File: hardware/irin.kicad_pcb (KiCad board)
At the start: 2 copper layers, 78.5 x 69 mm, 15 parts, among them J1 12V IN, J2 DHT22, U1 MP1584EN set to 5.0V, U2 01Space ESP32-C3-0.42LCD, U3 ADS1115 (HiLetgo)

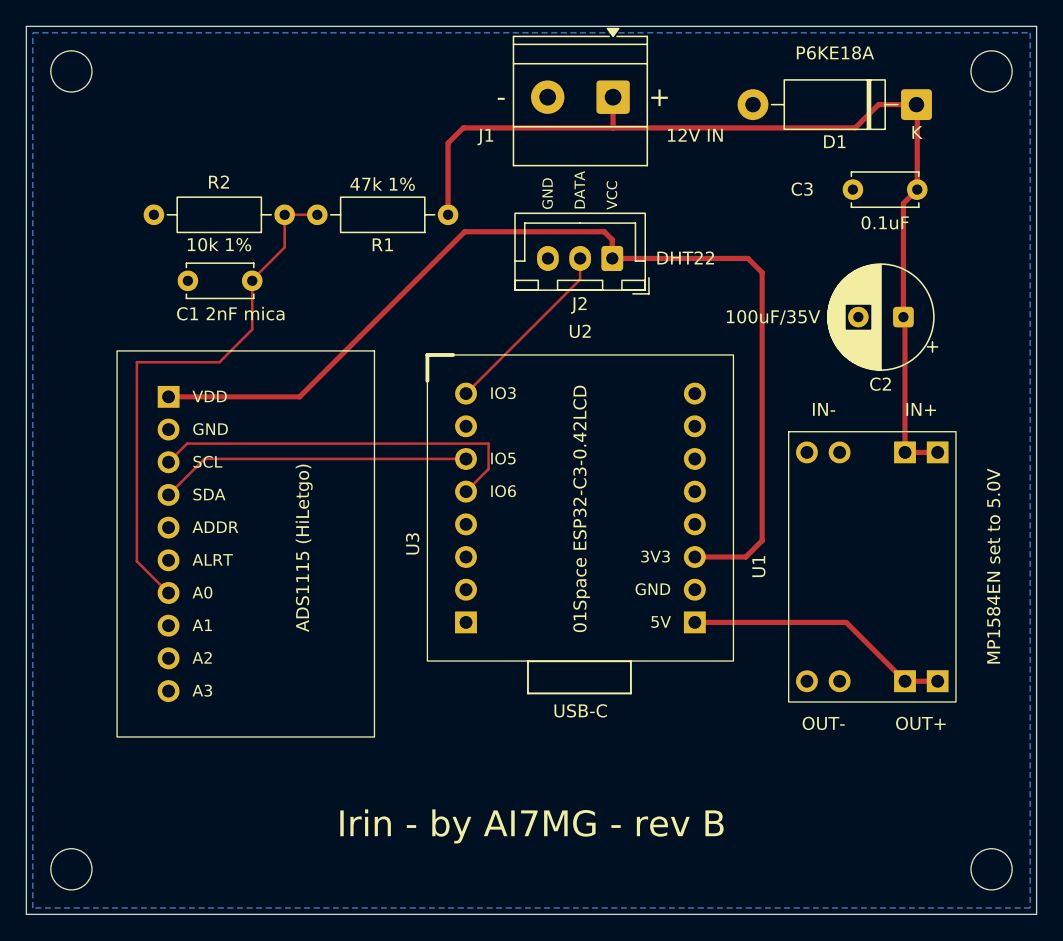
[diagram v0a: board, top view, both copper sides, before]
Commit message: Fix mirrored pad polarity in the U1 footprint
Second defect in the same footprint, found while reviewing the corrected
one: the '-' nets were on the left, which is backwards for a top-mounted
module. VIN+ and VOUT+ now sit on the left as the footprint is drawn,
viewed from the top, with the rectangular pads marking them.

On rev B board #1 the two defects cancelled. The workaround for the
too-narrow holes was to mount the module from the underside, which mirrors
the rows back -- which is why a board built on a wrong footprint runs
correctly, and why this was not caught electrically. A rev C board with U1
mounted normally on top would have fed IN+ into IN-.

Both footprint descriptions and the CLAUDE.md erratum updated.

Co-Authored-By: Claude Opus 5 <noreply@anthropic.com>
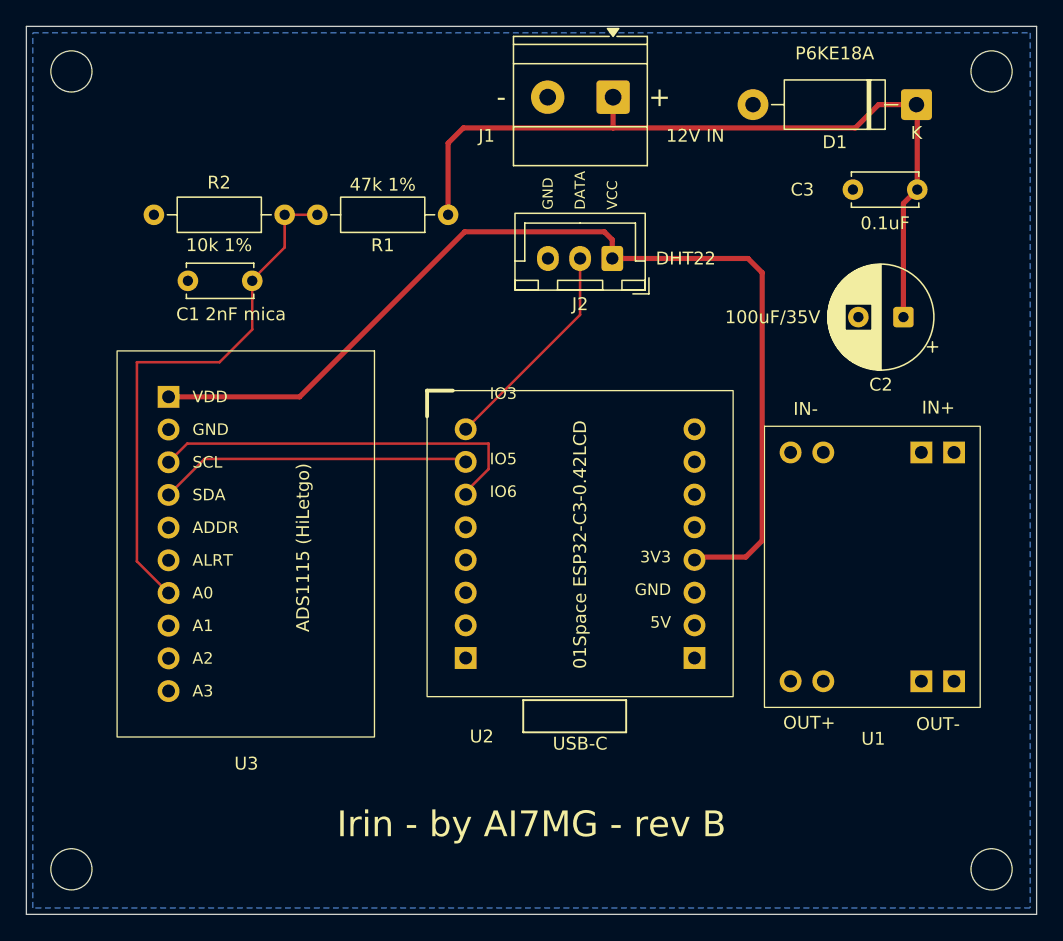
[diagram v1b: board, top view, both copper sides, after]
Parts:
- U1: footprint Irin:MP1584EN_HW133_2x2Pad_P2.54mm_W7.62mm_L17.78mm -> Irin:MP1584EN_HW133_2x2Pad_P2.54mm_W10.16mm_L17.78mm
- moved U2 2.77 mm to (43.6, 47.8)
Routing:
- net Net-(U1-OUT+): track 20.8 -> 0.00 mm
- net /12vPROT: track 75.4 -> 62.5 mm
- net Net-(J2-DATA): track 14.2 -> 16.9 mm
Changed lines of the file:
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@@
 		)
 	)
-	(footprint "Irin:MP1584EN_HW133_2x2Pad_P2.54mm_W7.62mm_L17.78mm"
+	(footprint "Irin:MP1584EN_HW133_2x2Pad_P2.54mm_W10.16mm_L17.78mm"
 		(layer "F.Cu")
 		(at 75.2348 58.4962)
-		(descr "MP1584EN adjustable buck module, HW-133A~F clone (silkscreen: 降压模块 / 输入 / 输出). 4 nets, each broken out to 2 redundant through-holes at 0.1in pitch: VIN-/VIN+ on one edge, VOUT-/VOUT+ on the opposite edge, 0.7in apart; the two net pairs on each edge are 0.3in apart center-to-center. Measured by owner with a ruler (input/output edge spacing and pair pitch only -- +/-0.5mm). Board outline below is NOT measured -- it is a generous placeholder box around the hole pattern for visual reference only. Pad numbers match the Irin:BUCK_MODULE schematic symbol (1=IN+ 2=IN- 3=OUT+ 4=OUT-). Rectangular pads mark the '+' nets (IN+, OUT+), matching the square pads printed on the real board next to its own '+' silkscreen -- also serves as the footprint's pin-1 indicator.")
+		(descr "MP1584EN adjustable buck module, HW-133A~F clone (silkscreen: 降压模块 / 输入 / 输出). 4 nets, each broken out to 2 redundant through-holes at 0.1in pitch: VIN-/VIN+ on one edge, VOUT-/VOUT+ on the opposite edge, 0.7in apart; the two net pairs on each edge are 0.4in apart center-to-center. CALIPER-MEASURED by owner 2026-10-20 on the physical module: taking one outer hole as 0, the four holes along an edge sit at 0.0 / 0.1 / 0.4 / 0.5 in, and the input edge to output edge spacing is 0.7 in. This CORRECTS Irin:MP1584EN_HW133_2x2Pad_P2.54mm_W7.62mm_L17.78mm, whose across-module spacing was ruler-measured at +/-0.5mm and came out 0.1in too narrow overall (inner holes at +/-0.2in apart instead of 0.3in); the real module does not fit that footprint -- see the rev B erratum in CLAUDE.md. Board outline CALIPER-MEASURED 2026-10-20 at 0.66 x 0.86 in = 16.76 x 21.84 mm (width across the hole rows x length between them), drawn true on F.SilkS; cross-checks against the hole pattern as 0.08 in of board margin on all four sides. Pad numbers match the Irin:BUCK_MODULE schematic symbol (1=IN+ 2=IN- 3=OUT+ 4=OUT-). Rectangular pads mark the '+' nets (IN+, OUT+), matching the square pads printed on the real board next to its own '+' silkscreen -- also serves as the footprint's pin-1 indicator.")
 		(tags "MP1584EN HW-133 buck module perfboard")
 		(property "Reference" "U1"
-			(at -8.787 -0.0208 90)
+			(at 0.0762 13.3604 0)
 			(layer "F.SilkS")
 			(effects
@@
 		)
 		(property "Value" "MP1584EN set to 5.0V"
-			(at 9.4652 0.0038 90)
-			(layer "F.SilkS")
+			(at 0 12.6 0)
+			(layer "F.Fab")
 			(effects
 				(font
@@
 		(sheetname "/")
 		(sheetfile "irin.kicad_sch")
-		(units
-			(unit
-				(name "A")
-				(pins "1" "2" "3" "4")
-			)
-		)
 		(attr through_hole)
 		(duplicate_pad_numbers_are_jumpers no)
 		(fp_rect
-			(start -6.5 -10.5)
-			(end 6.5 10.5)
+			(start -8.382 -10.922)
+			(end 8.382 10.922)
 			(stroke
 				(width 0.1)
@@
 		)
 		(fp_rect
-			(start -7 -11)
-			(end 7 11)
+			(start -8.882 -11.422)
+			(end 8.882 11.422)
 			(stroke
 				(width 0.05)
@@
 		)
 		(fp_text user "VIN-"
-			(at -3.81 -10.9 0)
+			(at -5.08 -10.2 0)
 			(layer "F.Fab")
 			(effects
@@
 		)
 		(fp_text user "VOUT-"
-			(at -3.81 10.9 0)
+			(at -5.08 10.2 0)
 			(layer "F.Fab")
 			(effects
@@
 		)
 		(fp_text user "VIN+"
-			(at 3.81 -10.9 0)
+			(at 5.08 -10.2 0)
 			(layer "F.Fab")
 			(effects
@@
 		)
 		(fp_text user "VOUT+"
-			(at 3.81 10.9 0)
+			(at 5.08 10.2 0)
 			(layer "F.Fab")
 			(effects
@@
 		)
 		(pad "1" thru_hole rect
-			(at 2.54 -8.89)
+			(at 3.81 -8.89)
 			(size 1.7 1.7)
 			(drill 1)
@@
 		)
 		(pad "1" thru_hole rect
-			(at 5.08 -8.89)
+			(at 6.35 -8.89)
 			(size 1.7 1.7)
 			(drill 1)
@@
 		)
 		(pad "2" thru_hole circle
-			(at -5.08 -8.89)
+			(at -6.35 -8.89)
 			(size 1.7 1.7)
 			(drill 1)
@@
 		)
 		(pad "2" thru_hole circle
-			(at -2.54 -8.89)
+			(at -3.81 -8.89)
 			(size 1.7 1.7)
 			(drill 1)
@@
 		)
 		(pad "3" thru_hole rect
-			(at 2.54 8.89)
+			(at 3.81 8.89)
 			(size 1.7 1.7)
 			(drill 1)
@@
 		)
 		(pad "3" thru_hole rect
-			(at 5.08 8.89)
+			(at 6.35 8.89)
 			(size 1.7 1.7)
 			(drill 1)
@@
 		)
 		(pad "4" thru_hole circle
-			(at -5.08 8.89)
+			(at -6.35 8.89)
 			(size 1.7 1.7)
 			(drill 1)
@@
 		)
 		(pad "4" thru_hole circle
-			(at -2.54 8.89)
+			(at -3.81 8.89)
 			(size 1.7 1.7)
 			(drill 1)
@@
 	(footprint "Irin:ESP32C3_042LCD_2x8_P2.54mm_W17.78mm"
 		(layer "F.Cu")
-		(at 43.6626 45.0342)
+		(at 43.6372 47.8028)
 		(descr "01Space ESP32-C3-0.42LCD dev board: 2x8 THT pin rows, 0.1in pitch, 0.7in row spacing. Pad numbers match the Irin:ESP32C3_BOARD schematic symbol (1=5V 2=3V3 3=GND 4=GPIO3 5=GPIO5 6=GPIO6); pads 7-16 are the board's other physical pins, not used in this design, numbered arbitrarily.")
 		(tags "ESP32-C3 01Space 0.42LCD perfboard")
 		(property "Reference" "U2"
-			(at 8.8852 -4.8008 0)
+			(at 1.2446 23.876 0)
 			(layer "F.SilkS")
 			(effects
@@
 		(tags "ADS1115 HiLetgo ADC breakout perfboard")
 		(property "Reference" "U3"
-			(at 0 -13 90)
+			(at 17.0688 -0.0452 180)
 			(layer "F.SilkS")
 			(effects
@@
 			)
 		)
+		(sheetname "/")
+		(sheetfile "irin.kicad_sch")
+		(units
+			(unit
+				(name "A")
+				(pins "1" "2")
+			)
+		)
 		(attr through_hole)
 		(duplicate_pad_numbers_are_jumpers no)
@@
 			(roundrect_rratio 0.096154)
 			(net "/12vPROT")
+			(pinfunction "BATT+_1")
+			(pintype "passive")
 		)
 		(pad "2" thru_hole circle
@@
 			(remove_unused_layers no)
 			(net "/GND")
+			(pinfunction "GND_2")
+			(pintype "passive")
 		)
 		(embedded_fonts no)
@@
 	)
 	(gr_rect
-		(start 48.4764 65.8314)
-		(end 56.4764 68.3314)
+		(start 48.1086 68.854)
+		(end 56.1086 71.354)
 		(stroke
 			(width 0.15)
@@
 	)
 	(gr_text "USB-C"
-		(at 52.5526 69.723 0)
+		(at 52.5272 72.2376 0)
 		(layer "F.SilkS")
 		(effects
@@
 	)
 	(gr_text "IN-"
-		(at 71.45 46.3 0)
+		(at 70.0532 46.228 0)
 		(layer "F.SilkS")
 		(effects
@@
 		)
 	)
-	(gr_text "OUT-"
-		(at 71.45 70.7 0)
+	(gr_text "OUT+"
+		(at 70.3326 70.612 0)
 		(layer "F.SilkS")
 		(effects
@@
 		)
 	)
-	(gr_text "IN+"
-		(at 79.04 46.3 0)
+	(gr_text "OUT-"
+		(at 80.3402 70.7136 0)
 		(layer "F.SilkS")
 		(effects
@@
 		)
 	)
-	(gr_text "OUT+"
-		(at 79.04 70.7 0)
+	(gr_text "IN+"
+		(at 80.3656 46.1264 0)
 		(layer "F.SilkS")
 		(effects
@@
 	)
 	(segment
-		(start 77.7748 49.6062)
-		(end 80.3148 49.6062)
-		(width 0.4)
-		(layer "F.Cu")
-		(net "/12vPROT")
-	)
-	(segment
 		(start 55.09 22)
 		(end 55.09 24.39)
@@
 	)
 	(segment
-		(start 77.7748 49.6062)
-		(end 77.7748 39.215949)
-		(width 0.4)
-		(layer "F.Cu")
-		(net "/12vPROT")
-	)
-	(segment
 		(start 42.2694 31.1404)
 		(end 42.2694 25.574)
@@
 	)
 	(segment
-		(start 73.2028 62.8142)
-		(end 61.4426 62.8142)
-		(width 0.4)
-		(layer "F.Cu")
-		(net "Net-(U1-OUT+)")
-	)
-	(segment
-		(start 77.7748 67.3862)
-		(end 73.2028 62.8142)
-		(width 0.4)
-		(layer "F.Cu")
-		(net "Net-(U1-OUT+)")
-	)
-	(segment
-		(start 80.3148 67.3862)
-		(end 77.7748 67.3862)
-		(width 0.4)
-		(layer "F.Cu")
-		(net "Net-(U1-OUT+)")
-	)
-	(segment
 		(start 66.675 35.6362)
 		(end 65.5744 34.5356)
@@
 	)
 	(segment
-		(start 43.6626 45.0342)
-		(end 52.5272 36.1696)
+		(start 52.5272 34.5356)
+		(end 52.5272 38.9128)
 		(width 0.2)
 		(layer "F.Cu")
@@
 	)
 	(segment
-		(start 52.5272 36.1696)
-		(end 52.5272 34.5356)
+		(start 52.5272 38.9128)
+		(end 43.6372 47.8028)
 		(width 0.2)
 		(layer "F.Cu")
@@
 		(polygon
 			(pts
-				(xy 40.3 38) (xy 64.8 38) (xy 64.8 44) (xy 40.3 44)
+				(xy 40.024226 44.0888) (xy 64.524226 44.0888) (xy 64.524226 50.0888) (xy 40.024226 50.0888)
 			)
 		)

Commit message: Board: mirror U1 pad polarity; silkscreen rework
The rev B board put + on the right at U1, but the real MP1584EN module has
- on the right. Update Footprints from Library pulled in the corrected
10.16mm hole spacing but predated the polarity fix, so the board kept the
old arrangement.

Mirrored U1's eight pad x-coordinates in place, which moves /12vPROT and
Net-(U1-OUT+) to the left and /GND to the right while leaving pad numbers,
nets, shapes and UUIDs alone. Verified against the library: all 8 pads now
match on position, shape, size and drill. The F.Fab VIN/VOUT labels in the
board instance were still reading the old way and are swapped to match.

Also includes the owner's silkscreen rework, including moving the U[n]
reference designators clear of the part bodies.

DRC still reports U1 as differing from its library footprint. That is the
silkscreen and text, not copper -- the pads are identical. Saving the
instance back to the library would clear it and stop a future Update
Footprints from discarding the label placement.

Co-Authored-By: Claude Opus 5 <noreply@anthropic.com>
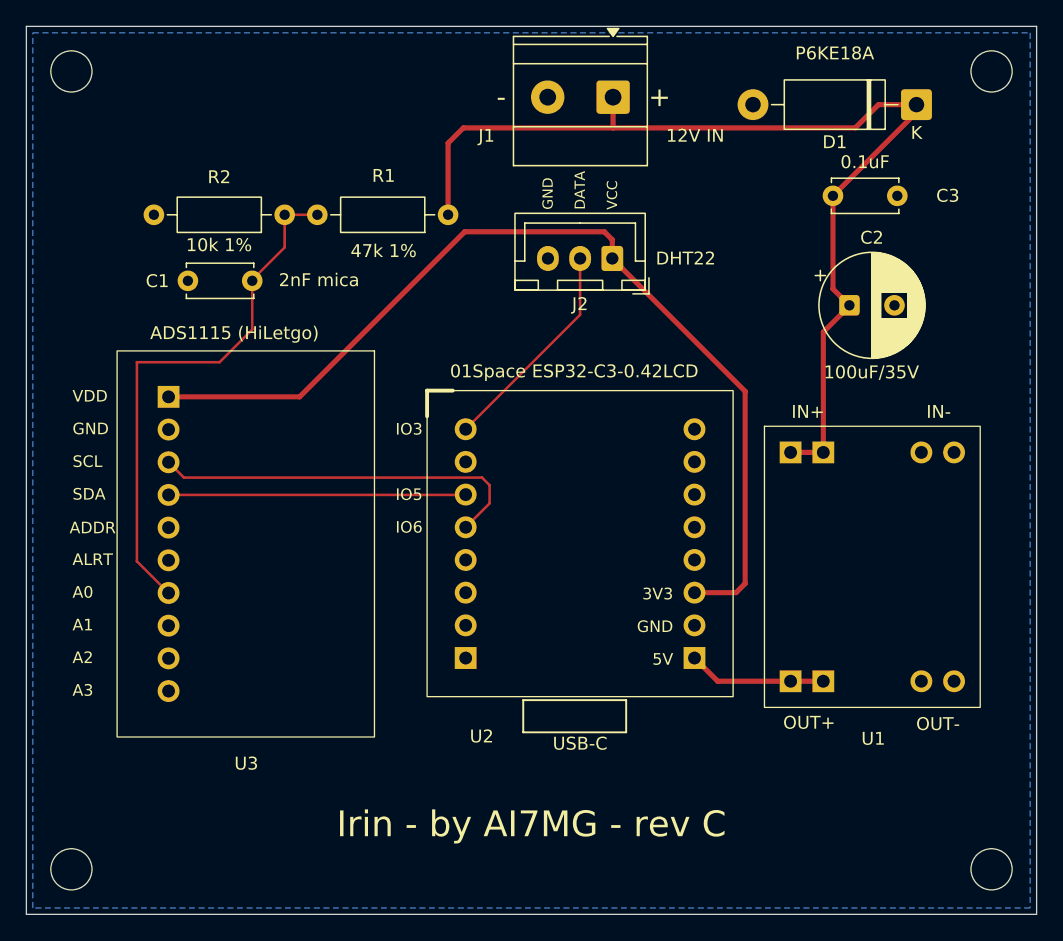
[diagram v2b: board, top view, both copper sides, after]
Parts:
- H1, H2, H3, H4: footprint MountingHole_3.2mm_M3 -> MountingHole:MountingHole_3.2mm_M3
- moved C3 6.57 mm to (72.2, 29.7), turned to 0 degrees
- moved C2 4.29 mm to (73.5, 38.2), turned to 0 degrees
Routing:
- net /12vPROT: track 62.5 -> 79.2 mm
- net Net-(U1-OUT+): track 0.00 -> 10.8 mm
- net Net-(J2-VCC): track 80.2 -> 75.3 mm
- net Net-(U2-GPIO5): track 24.3 -> 23.1 mm
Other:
- board text added: "Irin - by AI7MG - rev C"
- board text removed: "Irin - by AI7MG - rev B"
